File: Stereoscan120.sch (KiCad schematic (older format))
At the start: 2 parts

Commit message: Link up Power 343
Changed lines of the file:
@@
 F10 "P73" I R 13650 2300 60
 $EndSheet
+Wire Bus Line
+	2750 6000 2200 6000
+Text Label 2600 6000 2    60   ~ 0
+Power-343
+Wire Bus Line
+	13650 2150 14150 2150
+Text Label 13750 2150 0    60   ~ 0
+Power-343
 $EndSCHEMATC

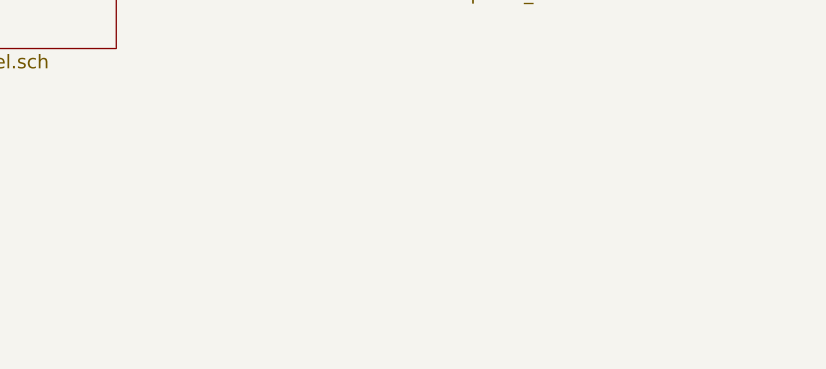
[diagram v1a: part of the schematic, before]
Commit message: Adds Collector Decoupling (potted)
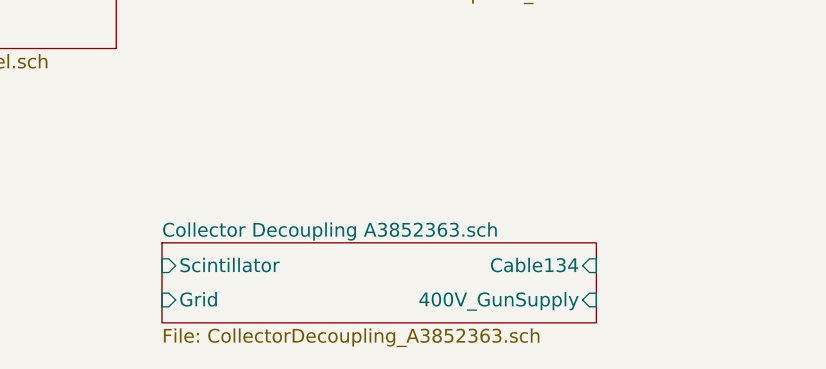
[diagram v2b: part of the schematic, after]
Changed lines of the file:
@@
 $Descr A3 16535 11693
 encoding utf-8
-Sheet 1 14
+Sheet 1 15
 Title ""
 Date ""
@@
 Text Label 13750 2150 0    60   ~ 0
 Power-343
+$Sheet
+S 2000 8250 1900 350
+U 5B0A26A0
+F0 "Collector Decoupling A3852363.sch" 60
+F1 "CollectorDecoupling_A3852363.sch" 60
+F2 "Scintillator" I L 2000 8350 60
+F3 "Grid" I L 2000 8500 60
+F4 "Cable134" I R 3900 8350 60
+F5 "400V_GunSupply" I R 3900 8500 60
+$EndSheet
 $EndSCHEMATC

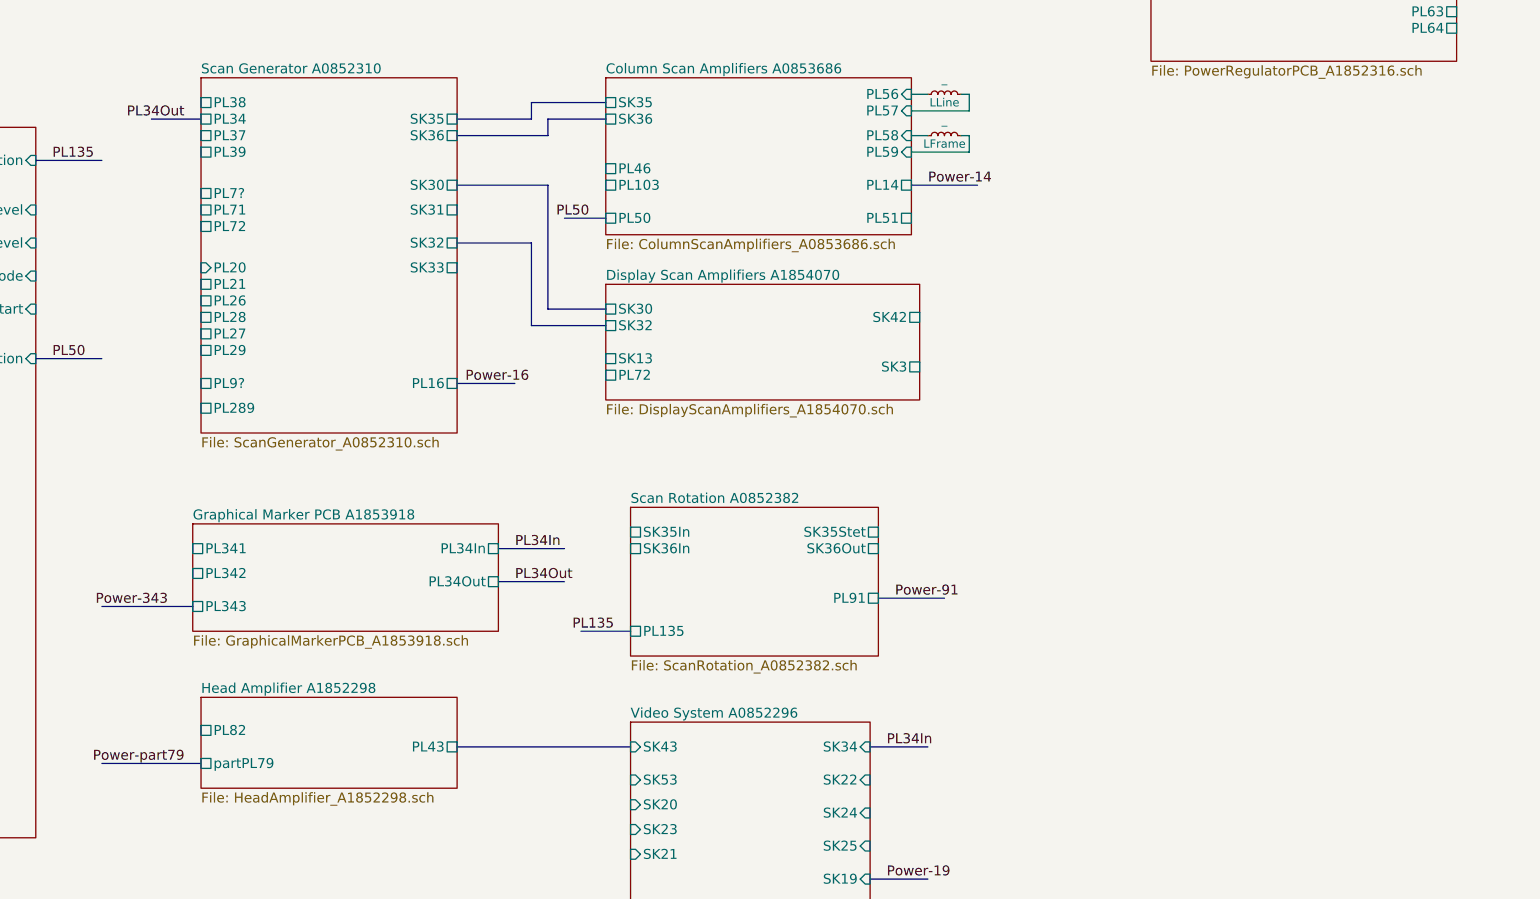
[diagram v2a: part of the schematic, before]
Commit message: Adds Video Processor PCB
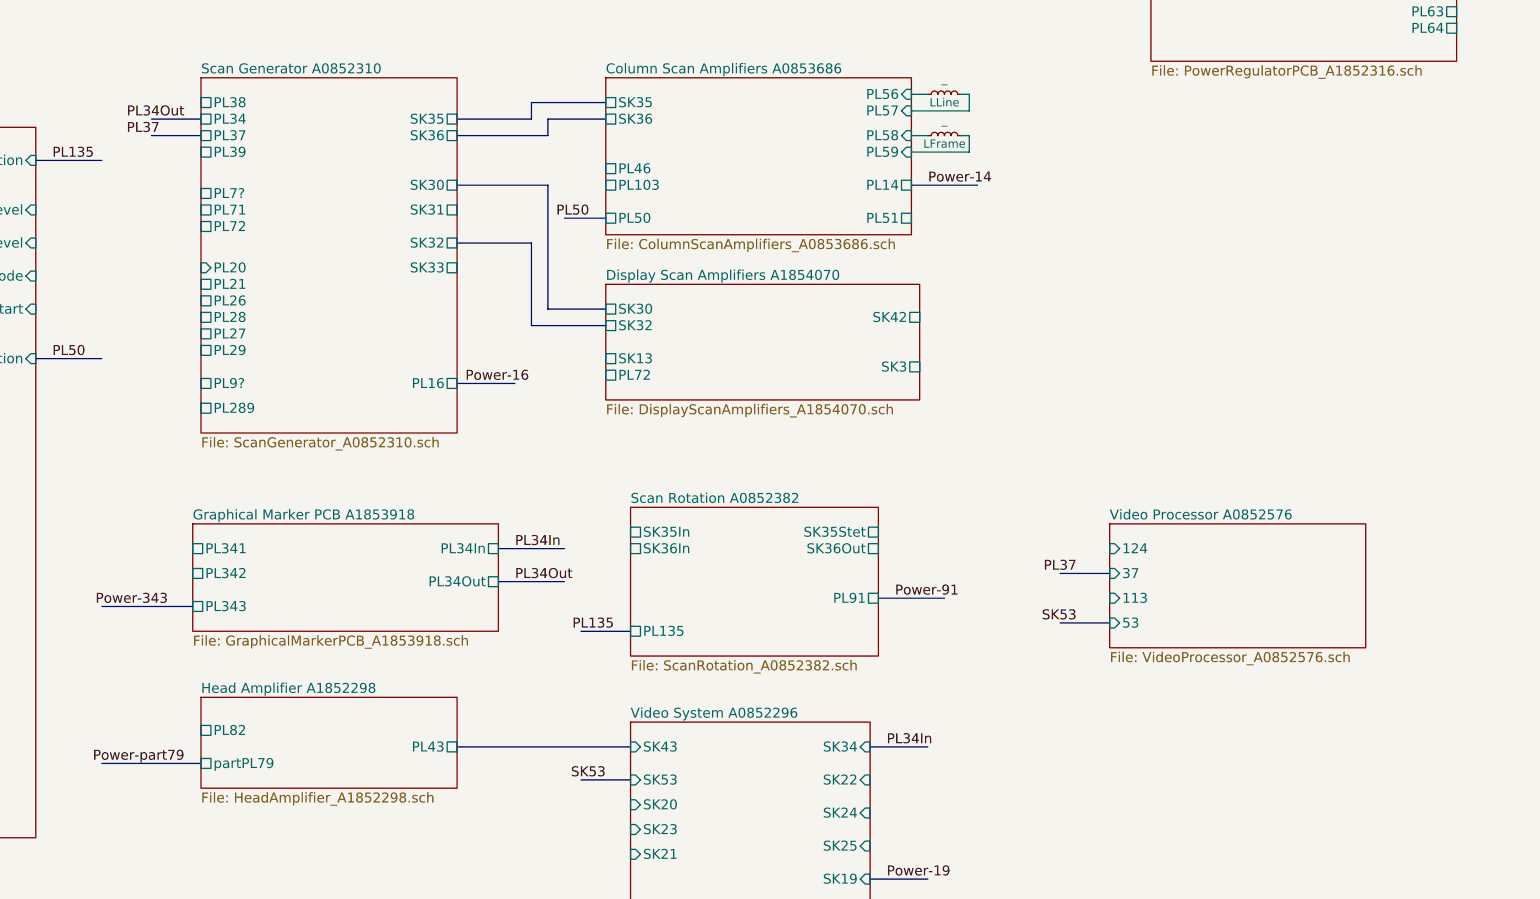
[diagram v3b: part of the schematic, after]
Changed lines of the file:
@@
 $Descr A3 16535 11693
 encoding utf-8
-Sheet 1 15
+Sheet 1 16
 Title ""
 Date ""
@@
 F5 "400V_GunSupply" I R 3900 8500 60
 $EndSheet
+$Sheet
+S 8300 5500 1550 750
+U 5B0B04E3
+F0 "Video Processor A0852576" 60
+F1 "VideoProcessor_A0852576.sch" 60
+F2 "124" I L 8300 5650 60
+F3 "37" I L 8300 5800 60
+F4 "113" I L 8300 5950 60
+F5 "53" I L 8300 6100 60
+$EndSheet
+Wire Bus Line
+	2800 3150 2500 3150
+Text Label 2550 3150 2    60   ~ 0
+PL37
+Wire Bus Line
+	8300 5800 8000 5800
+Text Label 8100 5800 2    60   ~ 0
+PL37
+Wire Bus Line
+	8300 6100 8000 6100
+Wire Bus Line
+	5400 7050 5100 7050
+Text Label 5250 7050 2    60   ~ 0
+SK53
+Text Label 8100 6100 2    60   ~ 0
+SK53
 $EndSCHEMATC

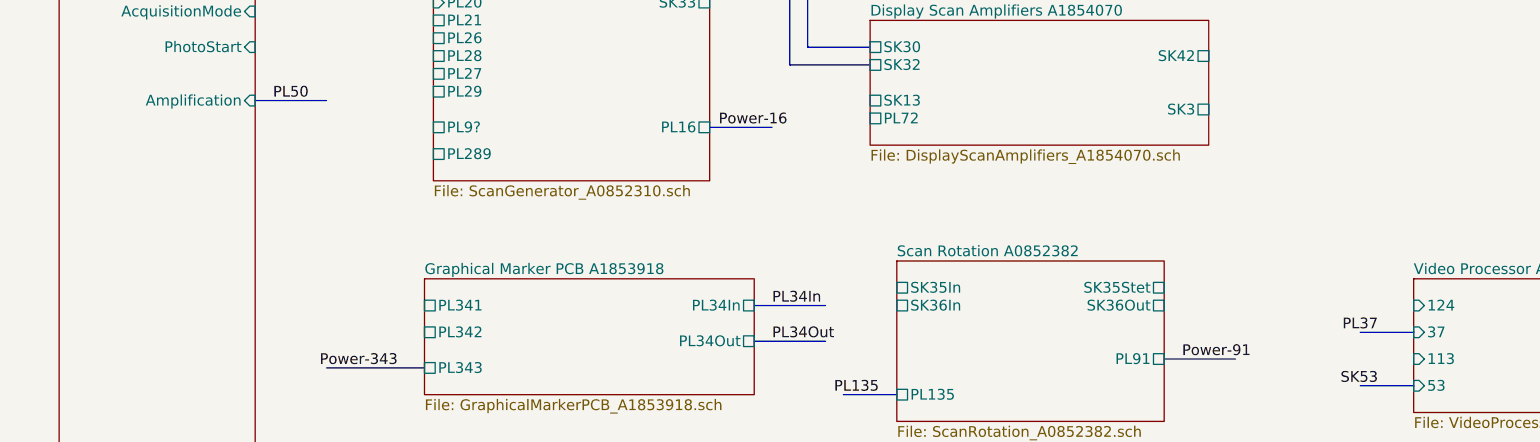
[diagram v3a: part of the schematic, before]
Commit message: Wires up Video Processor Front Panel Control
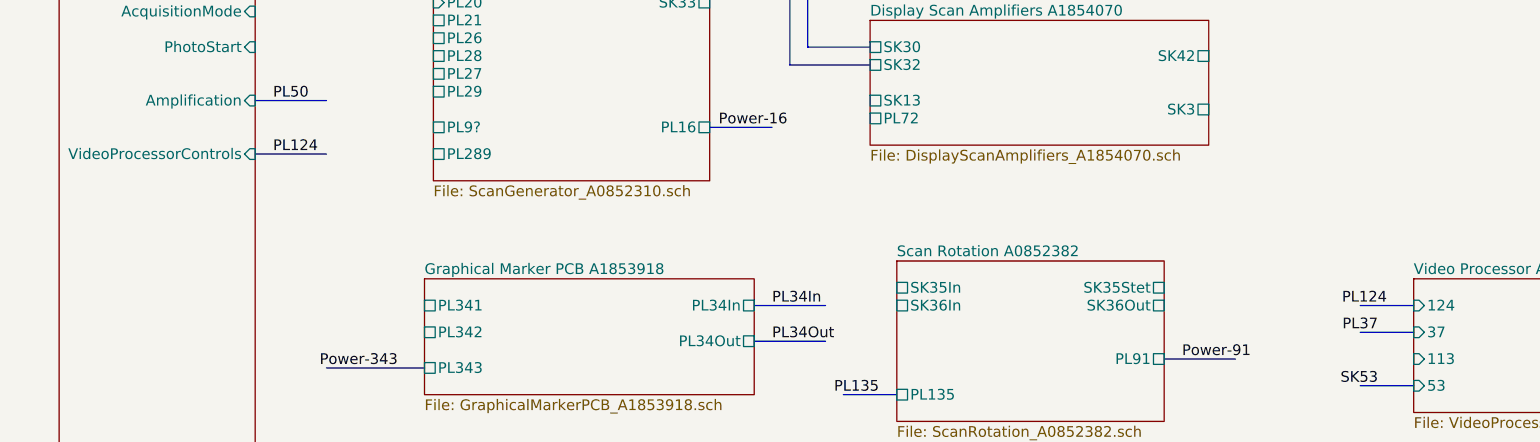
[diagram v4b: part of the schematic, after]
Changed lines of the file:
@@
 F6 "PhotoStart" I R 1800 4200 60
 F7 "Amplification" I R 1800 4500 60
+F8 "VideoProcessorControls" I R 1800 4800 60
 $EndSheet
 Text Label 1900 4500 0    60   ~ 0
@@
 Text Label 8100 6100 2    60   ~ 0
 SK53
+Wire Bus Line
+	1800 4800 2200 4800
+Text Label 1900 4800 0    60   ~ 0
+PL124
+Wire Bus Line
+	8300 5650 8000 5650
+Text Label 8150 5650 2    60   ~ 0
+PL124
 $EndSCHEMATC

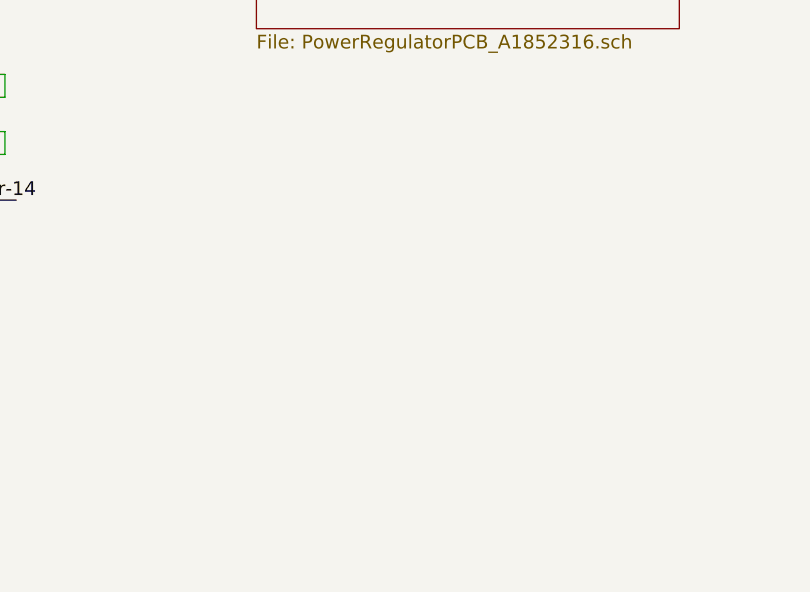
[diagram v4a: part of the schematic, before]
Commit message: Adds Electron Optics PCB
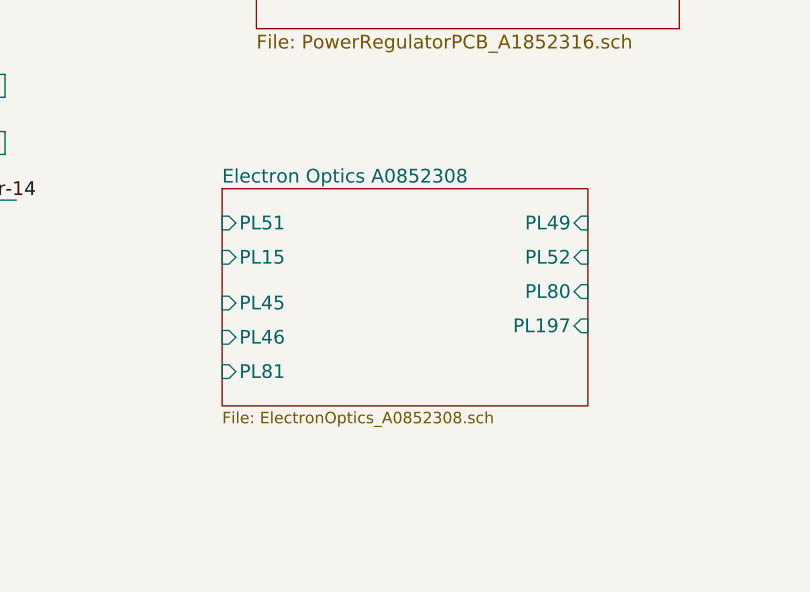
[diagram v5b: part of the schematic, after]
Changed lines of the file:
@@
 $Descr A3 16535 11693
 encoding utf-8
-Sheet 1 16
+Sheet 1 17
 Title ""
 Date ""
@@
 Text Label 8150 5650 2    60   ~ 0
 PL124
+$Sheet
+S 8400 3400 1600 950
+U 5B0CE4F6
+F0 "Electron Optics A0852308" 60
+F1 "ElectronOptics_A0852308.sch" 0
+F2 "PL51" I L 8400 3550 60
+F3 "PL45" I L 8400 3900 60
+F4 "PL49" I R 10000 3550 60
+F5 "PL15" I L 8400 3700 60
+F6 "PL80" I R 10000 3850 60
+F7 "PL81" I L 8400 4200 60
+F8 "PL197" I R 10000 4000 60
+F9 "PL46" I L 8400 4050 60
+F10 "PL52" I R 10000 3700 60
+$EndSheet
 $EndSCHEMATC

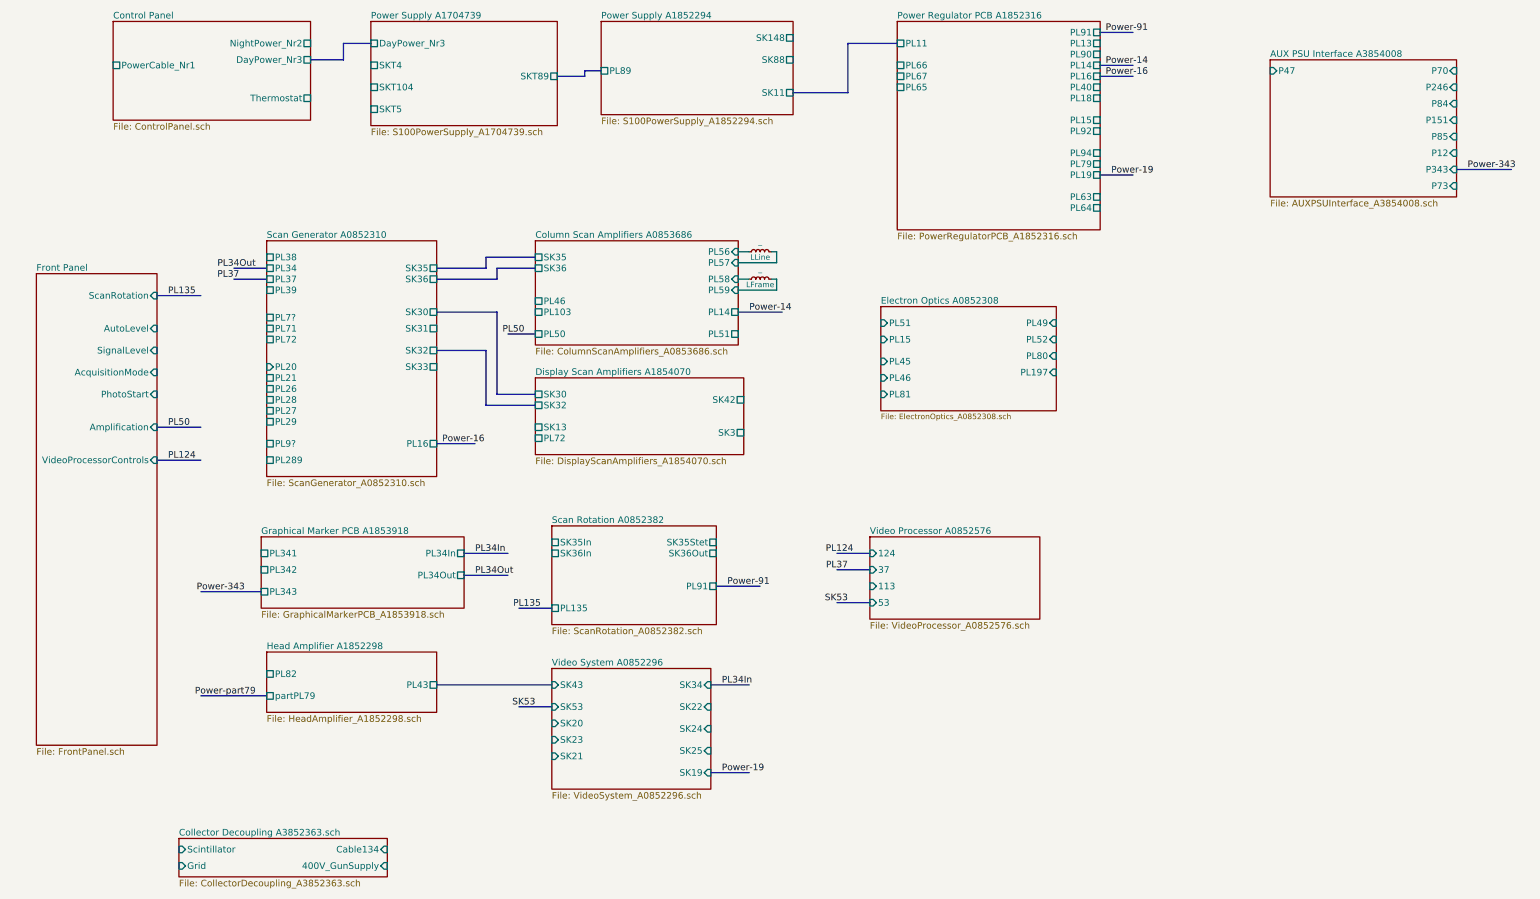
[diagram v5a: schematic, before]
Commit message: Wired up Electron Optics
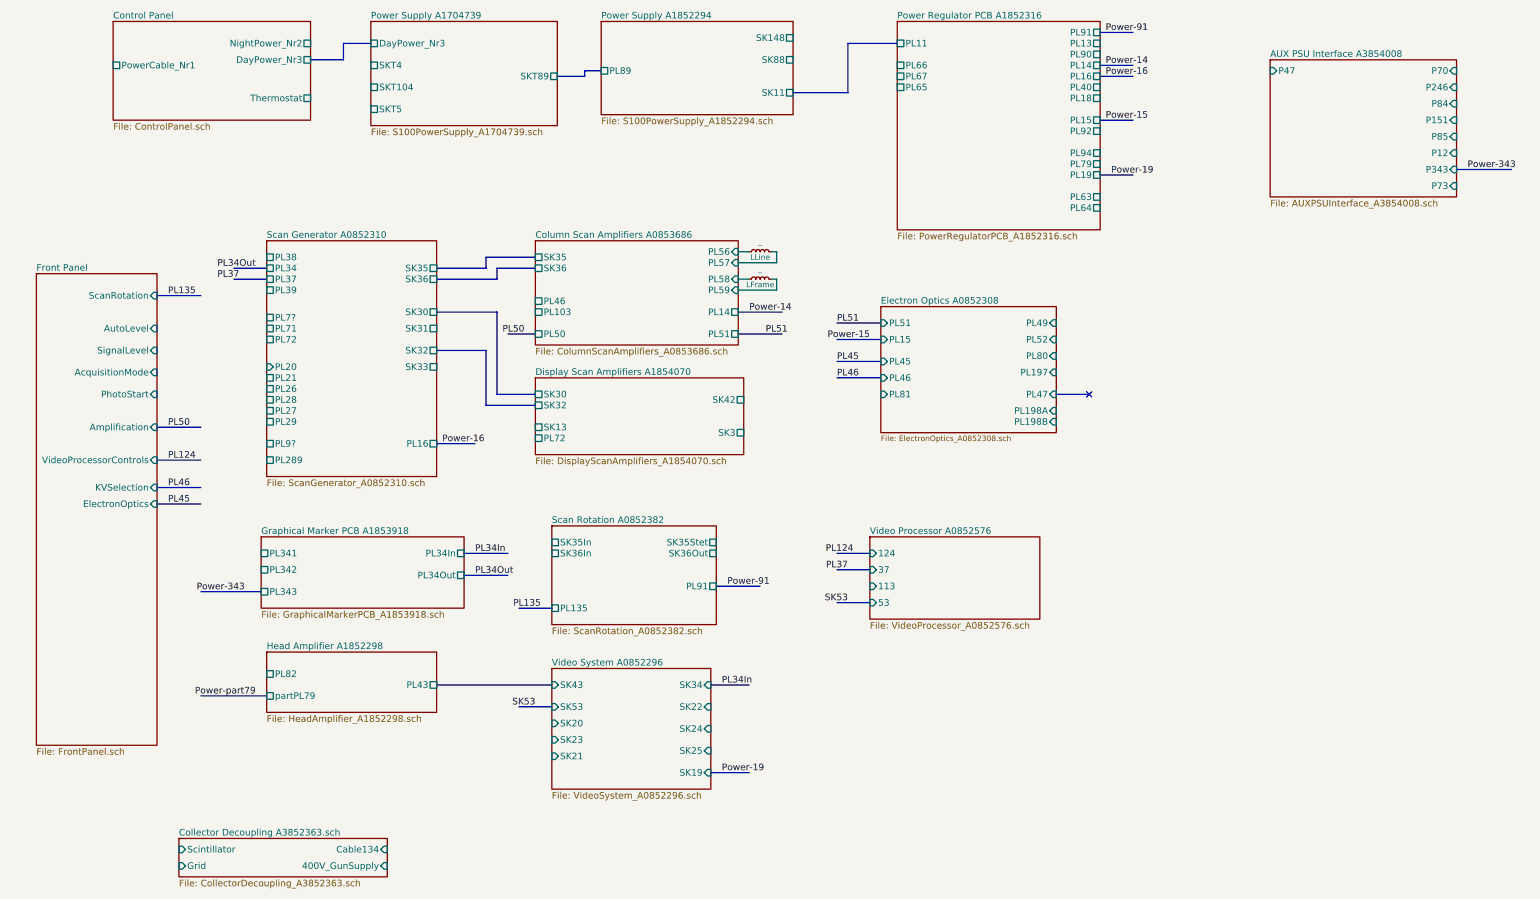
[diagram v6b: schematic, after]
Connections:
- no-connect marks 0 -> 1
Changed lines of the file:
@@
 F7 "Amplification" I R 1800 4500 60
 F8 "VideoProcessorControls" I R 1800 4800 60
+F9 "KVSelection" I R 1800 5050 60
+F10 "ElectronOptics" I R 1800 5200 60
 $EndSheet
 Text Label 1900 4500 0    60   ~ 0
@@
 PL124
 $Sheet
-S 8400 3400 1600 950
+S 8400 3400 1600 1150
 U 5B0CE4F6
 F0 "Electron Optics A0852308" 60
@@
 F9 "PL46" I L 8400 4050 60
 F10 "PL52" I R 10000 3700 60
-$EndSheet
+F11 "PL47" I R 10000 4200 60
+F12 "PL198A" I R 10000 4350 60
+F13 "PL198B" I R 10000 4450 60
+$EndSheet
+Wire Bus Line
+	8400 3550 8000 3550
+Text Label 8200 3550 2    60   ~ 0
+PL51
+Wire Bus Line
+	7100 3650 7500 3650
+Text Label 7350 3650 0    60   ~ 0
+PL51
+Wire Bus Line
+	10400 1700 10700 1700
+Text Label 10450 1700 0    60   ~ 0
+Power-15
+Wire Bus Line
+	8400 3700 8000 3700
+Text Label 8300 3700 2    60   ~ 0
+Power-15
+Wire Bus Line
+	1800 5050 2200 5050
+Wire Bus Line
+	1800 5200 2200 5200
+Text Label 1900 5050 0    60   ~ 0
+PL46
+Text Label 1900 5200 0    60   ~ 0
+PL45
+Wire Bus Line
+	8400 3900 8000 3900
+Wire Bus Line
+	8400 4050 8000 4050
+Text Label 8200 3900 2    60   ~ 0
+PL45
+Text Label 8200 4050 2    60   ~ 0
+PL46
+Wire Bus Line
+	10000 4200 10300 4200
+NoConn ~ 10300 4200
 $EndSCHEMATC
